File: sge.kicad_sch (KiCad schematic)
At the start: 20 parts, among them IC6 315-5660

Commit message: Start PCB layout.
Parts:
- C1, C2, C8: footprint (none) -> Capacitor_SMD:C_0805_2012Metric
- R3: footprint (none) -> Resistor_SMD:R_0805_2012Metric
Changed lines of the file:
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@@
       (effects (font (size 1.27 1.27)) (justify right))
     )
-    (property "Footprint" "" (at 147.193 256.54 90)
+    (property "Footprint" "Resistor_SMD:R_0805_2012Metric" (at 147.193 256.54 90)
       (effects (font (size 1.27 1.27)) hide)
     )
@@
       (effects (font (size 1.27 1.27)) (justify left))
     )
-    (property "Footprint" "" (at 262.5852 264.795 0)
+    (property "Footprint" "Capacitor_SMD:C_0805_2012Metric" (at 262.5852 264.795 0)
       (effects (font (size 1.27 1.27)) hide)
     )
@@
       (effects (font (size 1.27 1.27)) (justify right))
     )
-    (property "Footprint" "" (at 392.303 57.785 90)
+    (property "Footprint" "Resistor_SMD:R_0805_2012Metric" (at 392.303 57.785 90)
       (effects (font (size 1.27 1.27)) hide)
     )
@@
       (effects (font (size 1.27 1.27)) (justify left))
     )
-    (property "Footprint" "" (at 29.5148 178.435 0)
+    (property "Footprint" "Capacitor_SMD:C_0805_2012Metric" (at 29.5148 178.435 0)
       (effects (font (size 1.27 1.27)) hide)
     )
@@
       (effects (font (size 1.27 1.27)) (justify left))
     )
-    (property "Footprint" "" (at 60.6552 265.43 0)
+    (property "Footprint" "Capacitor_SMD:C_0805_2012Metric" (at 60.6552 265.43 0)
       (effects (font (size 1.27 1.27)) hide)
     )
@@
       (effects (font (size 1.27 1.27)) (justify right))
     )
-    (property "Footprint" "" (at 337.185 235.458 90)
+    (property "Footprint" "Resistor_SMD:R_0805_2012Metric" (at 337.185 235.458 90)
       (effects (font (size 1.27 1.27)) hide)
     )
@@
       (effects (font (size 1.27 1.27)) (justify left))
     )
-    (property "Footprint" "" (at 83.5152 265.43 0)
+    (property "Footprint" "Capacitor_SMD:C_0805_2012Metric" (at 83.5152 265.43 0)
       (effects (font (size 1.27 1.27)) hide)
     )
@@
       (effects (font (size 1.27 1.27)) (justify right))
     )
-    (property "Footprint" "" (at 392.303 195.58 90)
+    (property "Footprint" "Resistor_SMD:R_0805_2012Metric" (at 392.303 195.58 90)
       (effects (font (size 1.27 1.27)) hide)
     )
@@
       (effects (font (size 1.27 1.27)) (justify left))
     )
-    (property "Footprint" "" (at 36.5252 265.43 0)
+    (property "Footprint" "Capacitor_SMD:C_0805_2012Metric" (at 36.5252 265.43 0)
       (effects (font (size 1.27 1.27)) hide)
     )
@@
       (effects (font (size 1.27 1.27)) (justify right))
     )
-    (property "Footprint" "" (at 236.728 247.65 90)
+    (property "Footprint" "Resistor_SMD:R_0805_2012Metric" (at 236.728 247.65 90)
       (effects (font (size 1.27 1.27)) hide)
     )
@@
       (effects (font (size 1.27 1.27)) (justify left))
     )
-    (property "Footprint" "" (at 30.1498 75.565 0)
-      (effects (font (size 1.27 1.27)) hide)
-    )
+    (property "Footprint" "Capacitor_SMD:C_0805_2012Metric" (at 30.1498 75.565 0)
+      (effects (font (size 1.27 1.27)) hide)
+    )

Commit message: Save first mock-up before updating footprints.
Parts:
- removed RA1, RA3, RA4, RA5: 4x100, symbol Device:R_Pack04_SIP_Split
- added RA1, RA3, RA4, RA5: R_Pack04_Split, Resistor_SMD:R_Array_Convex_4x0603, symbol Device:R_Pack04_Split
- FB7: footprint (none) -> Inductor_SMD:L_0805_2012Metric
- RA2: value 4x100 -> R_Pack04_Split; footprint (none) -> Resistor_SMD:R_Array_Convex_4x0603
- RA6: value 2x100 -> R_Pack02_Split; footprint (none) -> Resistor_SMD:R_Array_Convex_2x0603
- RN1: footprint (none) -> Resistor_SMD:R_Array_Convex_4x0603
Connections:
- net AD0: now also RA3.1 (R1.1)
- net AD1: now also RA3.2 (R2.1)
- net AD2: now also RA3.3 (R3.1)
- net AD3: now also RA3.4 (R4.1)
- net AD4: now also RA4.1 (R1.1)
- net AD5: now also RA4.2 (R2.1)
- net AD6: now also RA4.3 (R3.1)
- net AD7: now also RA4.4 (R4.1)
- net SD0: now also RA1.1 (R1.1)
- net SD1: now also RA1.2 (R2.1)
- net SD2: now also RA1.3 (R3.1)
- net SD3: now also RA1.4 (R4.1)
- net SD4: now also RA2.1 (R1.1); no longer RA2.8 (R1.2)
- net SD5: now also RA2.2 (R2.1); no longer RA2.7 (R2.2)
- net SD6: now also RA2.3 (R3.1); no longer RA2.6 (R3.2)
- net SD7: now also RA2.4 (R4.1); no longer RA2.5 (R4.2)
- net ~{CAS1}: now also RA5.4 (R4.1)
- net ~{OE1}: now also RA6.2 (R2.1)
- net ~{RAS1}: now also RA5.3 (R3.1)
- net ~{SC}: now also RA5.2 (R2.1)
- net ~{SE0}: now also RA5.1 (R1.1); no longer RA6.4 (R1.2)
- net ~{WE0}: now also RA6.1 (R1.1); no longer RA6.3 (R2.2)
- net at IC6.4 (SD3): now also RA1.5 (R4.2)
- net at IC6.1 (SD0): now also RA1.8 (R1.2)
- net at IC6.10 (/SE0): now also RA5.8 (R1.2); no longer RA6.1 (R1.1)
- net at IC6.11 (/SC): now also RA5.7 (R2.2)
- net at IC6.12 (/RAS1): now also RA5.6 (R3.2)
- net at IC6.13 (/CAS1): now also RA5.5 (R4.2)
- net at IC6.15 (/WE0): now also RA6.4 (R1.2); no longer RA6.2 (R2.1)
- net at IC6.16 (/OE1): now also RA6.3 (R2.2)
- net at IC6.2 (SD1): now also RA1.7 (R2.2)
- net at IC6.26 (AD0): now also RA3.8 (R1.2)
- net at IC6.27 (AD1): now also RA3.7 (R2.2)
- net at IC6.28 (AD2): now also RA3.6 (R3.2)
- net at IC6.29 (AD3): now also RA3.5 (R4.2)
- net at IC6.3 (SD2): now also RA1.6 (R3.2)
- net at IC6.30 (AD4): now also RA4.8 (R1.2)
- net at IC6.31 (AD5): now also RA4.7 (R2.2)
- net at IC6.32 (AD6): now also RA4.6 (R3.2)
- net at IC6.33 (AD7): now also RA4.5 (R4.2)
- net at IC6.5 (SD4): now also RA2.8 (R1.2); no longer RA2.1 (R1.1)
- net at IC6.6 (SD5): now also RA2.7 (R2.2); no longer RA2.2 (R2.1)
- net at IC6.7 (SD6): now also RA2.6 (R3.2); no longer RA2.3 (R3.1)
- net at IC6.8 (SD7): now also RA2.5 (R4.2); no longer RA2.4 (R4.1)
- net SBCR: no longer names the net of IC6.131 (SBCR)
- no-connect marks 25 -> 26
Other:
- moved on the sheet: C1

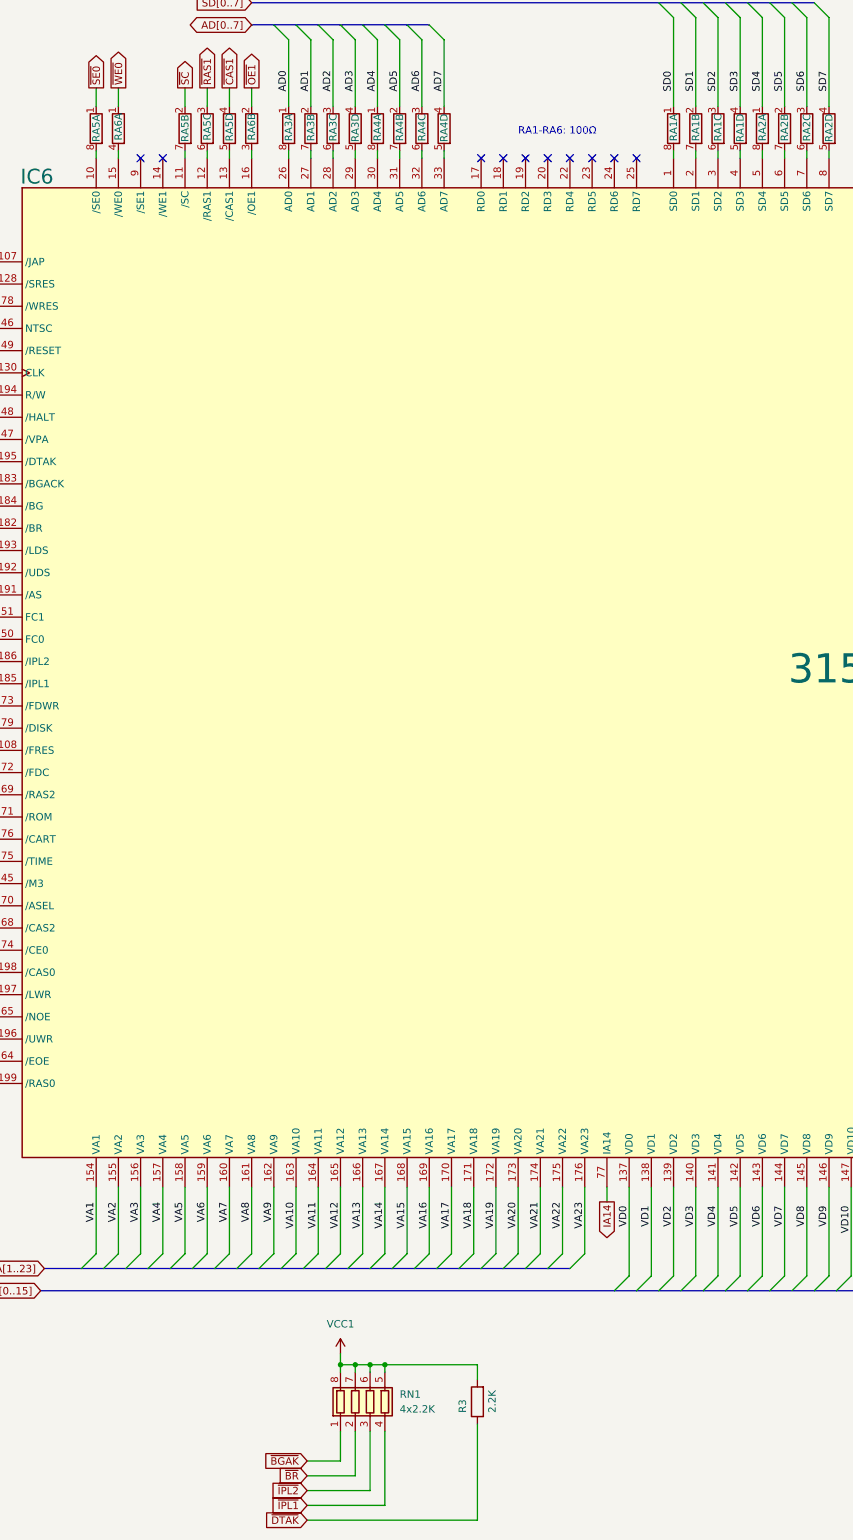
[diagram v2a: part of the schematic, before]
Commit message: Draft new layout with more accurate footprints.
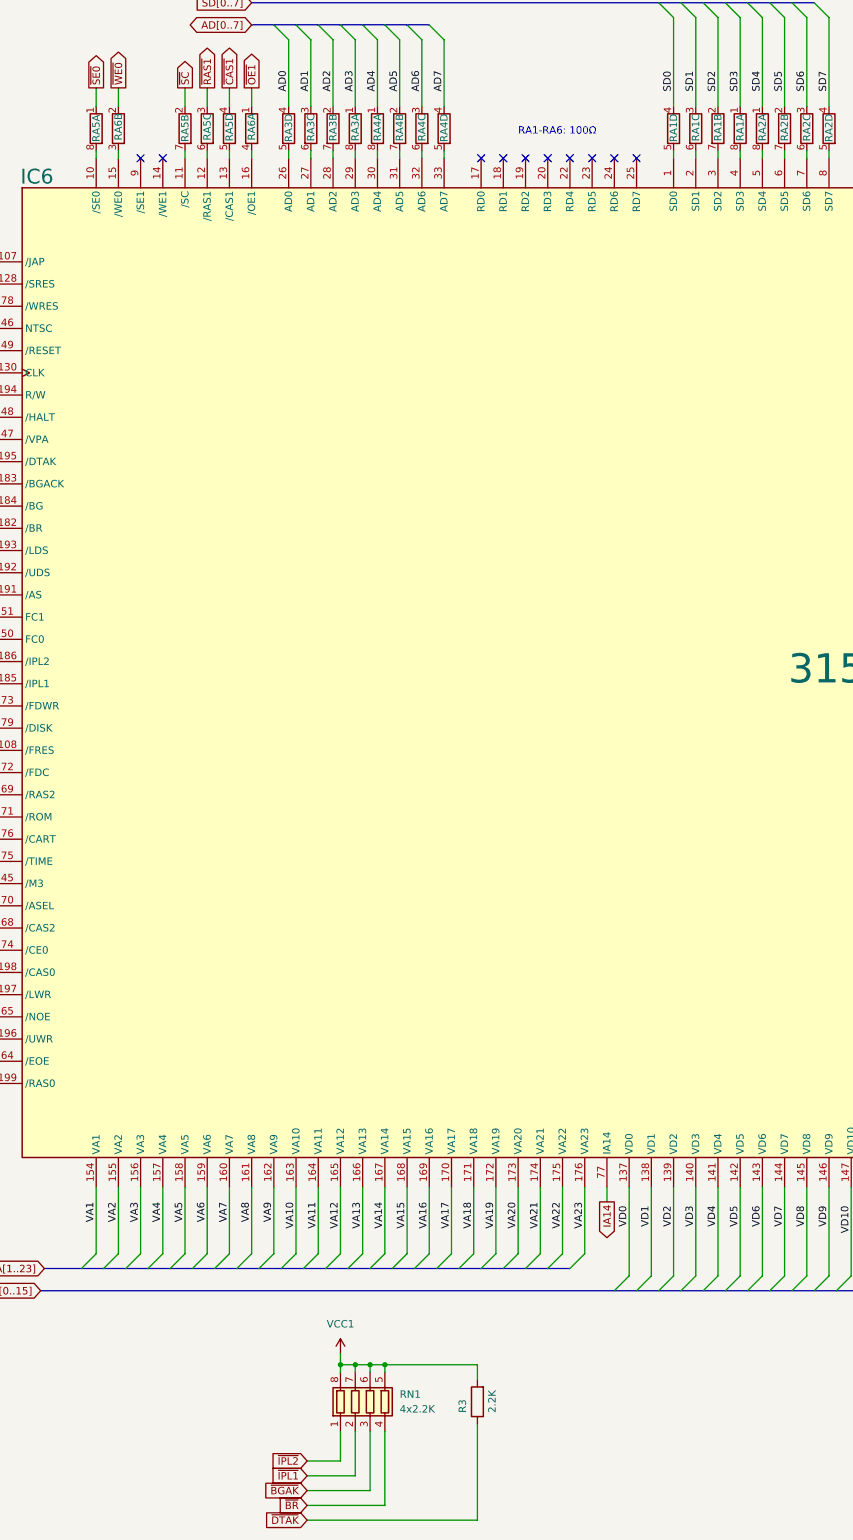
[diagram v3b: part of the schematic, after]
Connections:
- net AD0: now also RA3.4 (R4.1); no longer RA3.1 (R1.1)
- net AD1: now also RA3.3 (R3.1); no longer RA3.2 (R2.1)
- net AD2: now also RA3.2 (R2.1); no longer RA3.3 (R3.1)
- net AD3: now also RA3.1 (R1.1); no longer RA3.4 (R4.1)
- net SD0: now also RA1.4 (R4.1); no longer RA1.1 (R1.1)
- net SD1: now also RA1.3 (R3.1); no longer RA1.2 (R2.1)
- net SD2: now also RA1.2 (R2.1); no longer RA1.3 (R3.1)
- net SD3: now also RA1.1 (R1.1); no longer RA1.4 (R4.1)
- net ~{BGAK}: now also RN1.3 (R3.1); no longer RN1.1 (R1.1)
- net ~{BR}: now also RN1.4 (R4.1); no longer RN1.2 (R2.1)
- net ~{IPL1}: now also RN1.2 (R2.1); no longer RN1.4 (R4.1)
- net ~{IPL2}: now also RN1.1 (R1.1); no longer RN1.3 (R3.1)
- net ~{OE1}: now also RA6.1 (R1.1); no longer RA6.2 (R2.1)
- net ~{WE0}: now also RA6.2 (R2.1); no longer RA6.1 (R1.1)
- net at RA3.5 (R4.2): now also IC6.26 (AD0); no longer IC6.29 (AD3)
- net at IC6.1 (SD0): now also RA1.5 (R4.2); no longer RA1.8 (R1.2)
- net at IC6.15 (/WE0): now also RA6.3 (R2.2); no longer RA6.4 (R1.2)
- net at IC6.16 (/OE1): now also RA6.4 (R1.2); no longer RA6.3 (R2.2)
- net at IC6.2 (SD1): now also RA1.6 (R3.2); no longer RA1.7 (R2.2)
- net at RA3.8 (R1.2): now also IC6.29 (AD3); no longer IC6.26 (AD0)
- net at IC6.27 (AD1): now also RA3.6 (R3.2); no longer RA3.7 (R2.2)
- net at IC6.28 (AD2): now also RA3.7 (R2.2); no longer RA3.6 (R3.2)
- net at IC6.3 (SD2): now also RA1.7 (R2.2); no longer RA1.6 (R3.2)
- net at IC6.4 (SD3): now also RA1.8 (R1.2); no longer RA1.5 (R4.2)
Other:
- moved on the sheet: RA1A, RA1B, RA1C, RA1D, RA3A, RA3B, RA3C, RA3D, RA6A, RA6B

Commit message: Some power routing.
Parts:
- added C1: 22nF, Capacitor_SMD:C_0805_2012Metric, symbol Device:C
- added C912 (x2): 10uF, Capacitor_THT:CP_Radial_D5.0mm_P2.50mm, symbol Device:C_Polarized
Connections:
- net GND: now also C1.2, C912.2, C912.2
- net VCC1: now also C1.1, C912.1, C912.1
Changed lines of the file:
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@@
   (junction (at 121.92 250.19) (diameter 0) (color 0 0 0 0)
   )
+  (junction (at 264.16 231.775) (diameter 0) (color 0 0 0 0)
+  )
   (junction (at 314.96 243.84) (diameter 0) (color 0 0 0 0)
   )
@@
   (junction (at 323.85 255.27) (diameter 0) (color 0 0 0 0)
   )
+  (junction (at 278.13 243.84) (diameter 0) (color 0 0 0 0)
+  )
   (junction (at 129.54 250.19) (diameter 0) (color 0 0 0 0)
   )
@@
   (junction (at 261.62 254.635) (diameter 0) (color 0 0 0 0)
   )
+  (junction (at 278.13 231.775) (diameter 0) (color 0 0 0 0)
+  )
   (junction (at 297.18 222.25) (diameter 0) (color 0 0 0 0)
   )
@@
     (stroke (width 0) (type default))
   )
+  (wire (pts (xy 264.16 231.775) (xy 264.16 234.95))
+    (stroke (width 0) (type default))
+  )
   (wire (pts (xy 50.8 137.16) (xy 62.23 137.16))
     (stroke (width 0) (type default))
@@
     (stroke (width 0) (type default))
   )
+  (wire (pts (xy 278.13 242.57) (xy 278.13 243.84))
+    (stroke (width 0) (type default))
+  )
   (wire (pts (xy 273.05 219.71) (xy 273.05 231.775))
     (stroke (width 0) (type default))
@@
     (stroke (width 0) (type default))
   )
+  (wire (pts (xy 278.13 231.775) (xy 278.13 234.95))
+    (stroke (width 0) (type default))
+  )
   (wire (pts (xy 50.8 152.4) (xy 62.23 152.4))
     (stroke (width 0) (type default))
@@
     (stroke (width 0) (type default))
   )
+  (wire (pts (xy 264.16 243.84) (xy 278.13 243.84))
+    (stroke (width 0) (type default))
+  )
   (wire (pts (xy 273.05 231.775) (xy 270.51 231.775))
     (stroke (width 0) (type default))
@@
     (stroke (width 0) (type default))
   )
+  (wire (pts (xy 264.16 242.57) (xy 264.16 243.84))
+    (stroke (width 0) (type default))
+  )
   (wire (pts (xy 285.75 26.67) (xy 285.75 43.18))
     (stroke (width 0) (type default))
@@
     (stroke (width 0) (type default))
   )
+  (wire (pts (xy 170.18 257.81) (xy 170.18 261.62))
+    (stroke (width 0) (type default))
+  )
   (wire (pts (xy 50.8 68.58) (xy 62.23 68.58))
     (stroke (width 0) (type default))
@@
     (stroke (width 0) (type default))
   )
+  (wire (pts (xy 278.13 243.84) (xy 278.13 245.11))
+    (stroke (width 0) (type default))
+  )
   (bus (pts (xy 382.27 139.7) (xy 382.27 143.51))
     (stroke (width 0) (type default))
@@
     (stroke (width 0) (type default))
   )
+  (wire (pts (xy 170.18 269.24) (xy 170.18 273.685))
+    (stroke (width 0) (type default))
+  )
   (wire (pts (xy 186.69 19.05) (xy 186.69 34.29))
     (stroke (width 0) (type default))
@@
     )
   )
+  (symbol (lib_id "power:GND") (at 170.18 273.685 0) (unit 1)
+    (in_bom yes) (on_board yes) (dnp no) (fields_autoplaced)
+    (property "Reference" "#PWR0170" (at 170.18 280.035 0)
+      (effects (font (size 1.27 1.27)) hide)
+    )
+    (property "Value" "GND" (at 170.18 278.765 0)
+      (effects (font (size 1.27 1.27)))
+    )
+    (property "Footprint" "" (at 170.18 273.685 0)
+      (effects (font (size 1.27 1.27)) hide)
+    )
+    (property "Datasheet" "" (at 170.18 273.685 0)
+      (effects (font (size 1.27 1.27)) hide)
+    )
+    (pin "1")
+    (instances
+      (project "Neptune"
+        (path "/bcc23b51-b742-4ae5-9dd6-d96a24058944/0d895458-d3d0-4635-bde5-e15500822f5f"
+          (reference "#PWR0170") (unit 1)
+        )
+      )
+    )
+  )
+  (symbol (lib_id "Device:C_Polarized") (at 264.16 238.76 0) (unit 1)
+    (in_bom yes) (on_board yes) (dnp no)
+    (property "Reference" "C912" (at 256.54 241.3 90)
+      (effects (font (size 1.27 1.27)) (justify left))
+    )
+    (property "Value" "10uF" (at 259.08 241.3 90)
+      (effects (font (size 1.27 1.27)) (justify left))
+    )
+    (property "Footprint" "Capacitor_THT:CP_Radial_D5.0mm_P2.50mm" (at 265.1252 242.57 0)
+      (effects (font (size 1.27 1.27)) hide)
+    )
+    (property "Datasheet" "~" (at 264.16 238.76 0)
+      (effects (font (size 1.27 1.27)) hide)
+    )
+    (pin "1")
+    (pin "2")
+    (instances
+      (project "Neptune"
+        (path "/bcc23b51-b742-4ae5-9dd6-d96a24058944/01513199-62c5-4123-a151-ccd381a5e6c1"
+          (reference "C912") (unit 1)
+        )
+        (path "/bcc23b51-b742-4ae5-9dd6-d96a24058944/293c8f1f-2c58-4557-aeb8-8502bb66fbd4"
+          (reference "CE21") (unit 1)
+        )
+        (path "/bcc23b51-b742-4ae5-9dd6-d96a24058944/48e60f61-77cc-4ea0-898f-0029aa970ca5"
+          (reference "CE20") (unit 1)
+        )
+        (path "/bcc23b51-b742-4ae5-9dd6-d96a24058944/0d895458-d3d0-4635-bde5-e15500822f5f"
+          (reference "C30") (unit 1)
+        )
+      )
+    )
+  )
   (symbol (lib_id "Device:R_Pack04_Split") (at 198.12 38.1 0) (mirror x) (unit 2)
     (in_bom yes) (on_board yes) (dnp no)
@@
     )
   )
+  (symbol (lib_id "power:GND") (at 278.13 245.11 0) (unit 1)
+    (in_bom yes) (on_board yes) (dnp no) (fields_autoplaced)
+    (property "Reference" "#PWR0168" (at 278.13 251.46 0)
+      (effects (font (size 1.27 1.27)) hide)
+    )
+    (property "Value" "GND" (at 278.13 250.19 0)
+      (effects (font (size 1.27 1.27)))
+    )
+    (property "Footprint" "" (at 278.13 245.11 0)
+      (effects (font (size 1.27 1.27)) hide)
+    )
+    (property "Datasheet" "" (at 278.13 245.11 0)
+      (effects (font (size 1.27 1.27)) hide)
+    )
+    (pin "1")
+    (instances
+      (project "Neptune"
+        (path "/bcc23b51-b742-4ae5-9dd6-d96a24058944/0d895458-d3d0-4635-bde5-e15500822f5f"
+          (reference "#PWR0168") (unit 1)
+        )
+      )
+    )
+  )
   (symbol (lib_id "Device:C") (at 261.62 260.985 0) (unit 1)
     (in_bom yes) (on_board yes) (dnp no) (fields_autoplaced)
@@
     )
   )
+  (symbol (lib_id "Device:C") (at 170.18 265.43 0) (unit 1)
+    (in_bom yes) (on_board yes) (dnp no) (fields_autoplaced)
+    (property "Reference" "C1" (at 173.99 264.16 0)
+      (effects (font (size 1.27 1.27)) (justify left))
+    )
+    (property "Value" "22nF" (at 173.99 266.7 0)
+      (effects (font (size 1.27 1.27)) (justify left))
+    )
+    (property "Footprint" "Capacitor_SMD:C_0805_2012Metric" (at 171.1452 269.24 0)
+      (effects (font (size 1.27 1.27)) hide)
+    )
+    (property "Datasheet" "~" (at 170.18 265.43 0)
+      (effects (font (size 1.27 1.27)) hide)
+    )
+    (pin "1")
+    (pin "2")
+    (instances
+      (project "Neptune"
+        (path "/bcc23b51-b742-4ae5-9dd6-d96a24058944/01513199-62c5-4123-a151-ccd381a5e6c1"
+          (reference "C1") (unit 1)
+        )
+        (path "/bcc23b51-b742-4ae5-9dd6-d96a24058944/0d895458-d3d0-4635-bde5-e15500822f5f"
+          (reference "C32") (unit 1)
+        )
+      )
+    )
+  )
   (symbol (lib_id "MegaDrive:VCC1") (at 234.95 241.3 0) (unit 1)
     (in_bom yes) (on_board yes) (dnp no) (fields_autoplaced)
@@
     )
   )
+  (symbol (lib_id "MegaDrive:VCC1") (at 170.18 257.81 0) (unit 1)
+    (in_bom yes) (on_board yes) (dnp no) (fields_autoplaced)
+    (property "Reference" "#PWR01" (at 170.18 261.62 0)
+      (effects (font (size 1.27 1.27)) hide)
+    )
+    (property "Value" "VCC1" (at 170.18 252.73 0)
+      (effects (font (size 1.27 1.27)))
+    )
+    (property "Footprint" "" (at 170.18 257.81 0)
+      (effects (font (size 1.27 1.27)) hide)
+    )
+    (property "Datasheet" "" (at 170.18 257.81 0)
+      (effects (font (size 1.27 1.27)) hide)
+    )
+    (pin "1")
+    (instances
+      (project "Neptune"
+        (path "/bcc23b51-b742-4ae5-9dd6-d96a24058944"
+          (reference "#PWR01") (unit 1)
+        )
+        (path "/bcc23b51-b742-4ae5-9dd6-d96a24058944/48e60f61-77cc-4ea0-898f-0029aa970ca5"
+          (reference "#PWR01") (unit 1)
+        )
+        (path "/bcc23b51-b742-4ae5-9dd6-d96a24058944/0d895458-d3d0-4635-bde5-e15500822f5f"
+          (reference "#PWR0169") (unit 1)
+        )
+      )
+    )
+  )
   (symbol (lib_id "Device:C") (at 292.735 248.92 0) (unit 1)
     (in_bom yes) (on_board yes) (dnp no) (fields_autoplaced)
@@
         )
       )
+    )
+  )
+  (symbol (lib_id "Device:C_Polarized") (at 278.13 238.76 0) (unit 1)
+    (in_bom yes) (on_board yes) (dnp no)
+    (property "Reference" "C912" (at 270.51 241.3 90)
+      (effects (font (size 1.27 1.27)) (justify left))
+    )
+    (property "Value" "10uF" (at 273.05 241.3 90)
+      (effects (font (size 1.27 1.27)) (justify left))
+    )
+    (property "Footprint" "Capacitor_THT:CP_Radial_D5.0mm_P2.50mm" (at 279.0952 242.57 0)
+      (effects (font (size 1.27 1.27)) hide)
+    )
+    (property "Datasheet" "~" (at 278.13 238.76 0)
+      (effects (font (size 1.27 1.27)) hide)
+    )
+    (pin "1")
+    (pin "2")
+    (instances
+      (project "Neptune"
+        (path "/bcc23b51-b742-4ae5-9dd6-d96a24058944/01513199-62c5-4123-a151-ccd381a5e6c1"
+          (reference "C912") (unit 1)
+        )
+        (path "/bcc23b51-b742-4ae5-9dd6-d96a24058944/293c8f1f-2c58-4557-aeb8-8502bb66fbd4"
+          (reference "CE21") (unit 1)
+        )
+        (path "/bcc23b51-b742-4ae5-9dd6-d96a24058944/48e60f61-77cc-4ea0-898f-0029aa970ca5"
+          (reference "CE20") (unit 1)
+        )
+        (path "/bcc23b51-b742-4ae5-9dd6-d96a24058944/0d895458-d3d0-4635-bde5-e15500822f5f"
+          (reference "C29") (unit 1)
+        )
+      )
